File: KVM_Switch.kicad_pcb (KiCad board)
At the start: 4 copper layers, 100 x 70 mm, 118 parts, among them J1 HDMI_A, J2 HDMI_A, J3 HDMI_A, J4 USB_C_Receptacle_USB2.0_16P, J5 USB_C_Receptacle_USB2.0_16P, J6 USB_C_Receptacle_USB2.0_16P, J7 USB_A_Stacked, J8 USB_A_Stacked, SW1 SPST-NO, U1 TPD4E02B04DQA, U10 HD3SS215RTQR, U11 TLV75533PDBV, U12 STM32C031G6Ux, U13 USBLC6-2SC6, U14 TS3USB221AQRSERQ1, U15 USBLC6-2SC6, U16 USB2514B_Bi, U17 USBLC6-2SC6, U18 USBLC6-2SC6, U19 USBLC6-2SC6, U2 TPD4E02B04DQA, U20 USBLC6-2SC6, U3 TPD4E02B04DQA, U4 TPD4E02B04DQA, U5 TPD4E02B04DQA, U6 TPD4E02B04DQA, U7 TPD4E02B04DQA, U8 TPD4E02B04DQA, U9 TPD4E02B04DQA, X1 24MHz

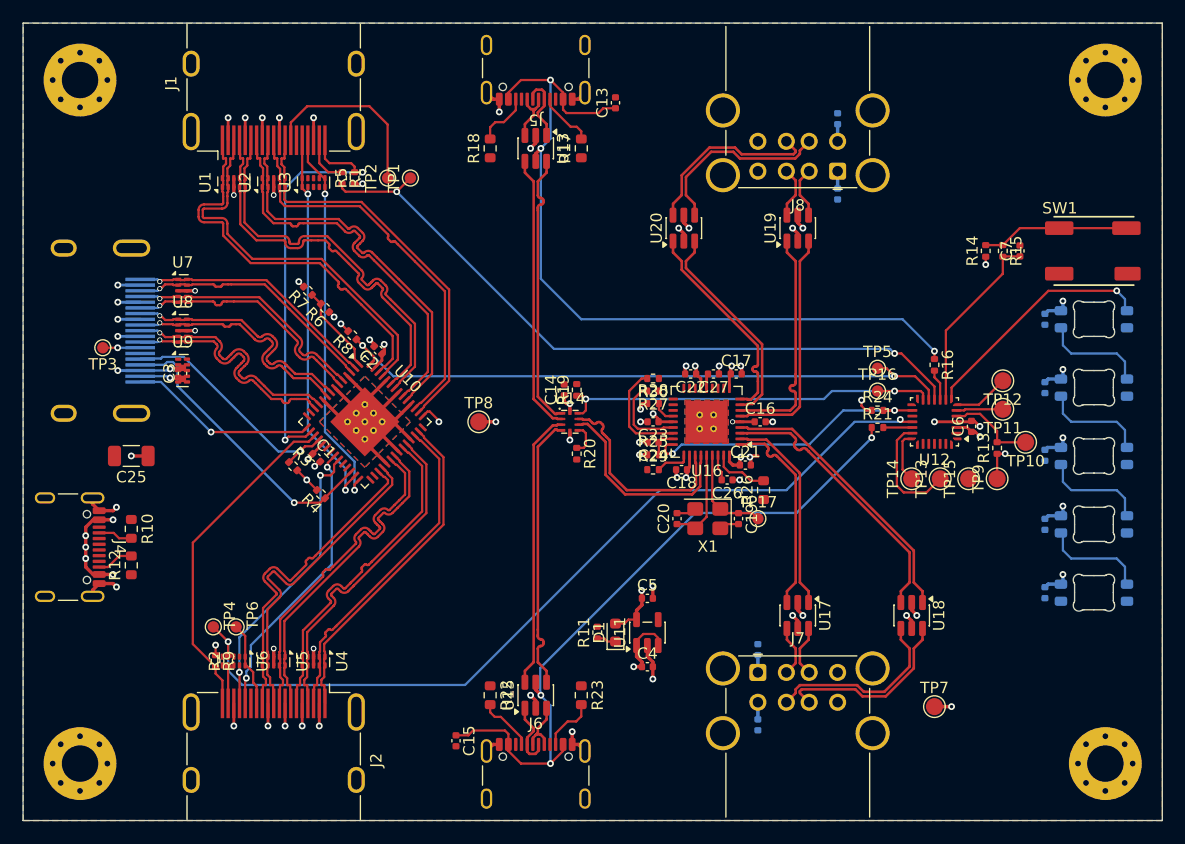
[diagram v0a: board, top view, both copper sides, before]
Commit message: Routed remaining ESD protection
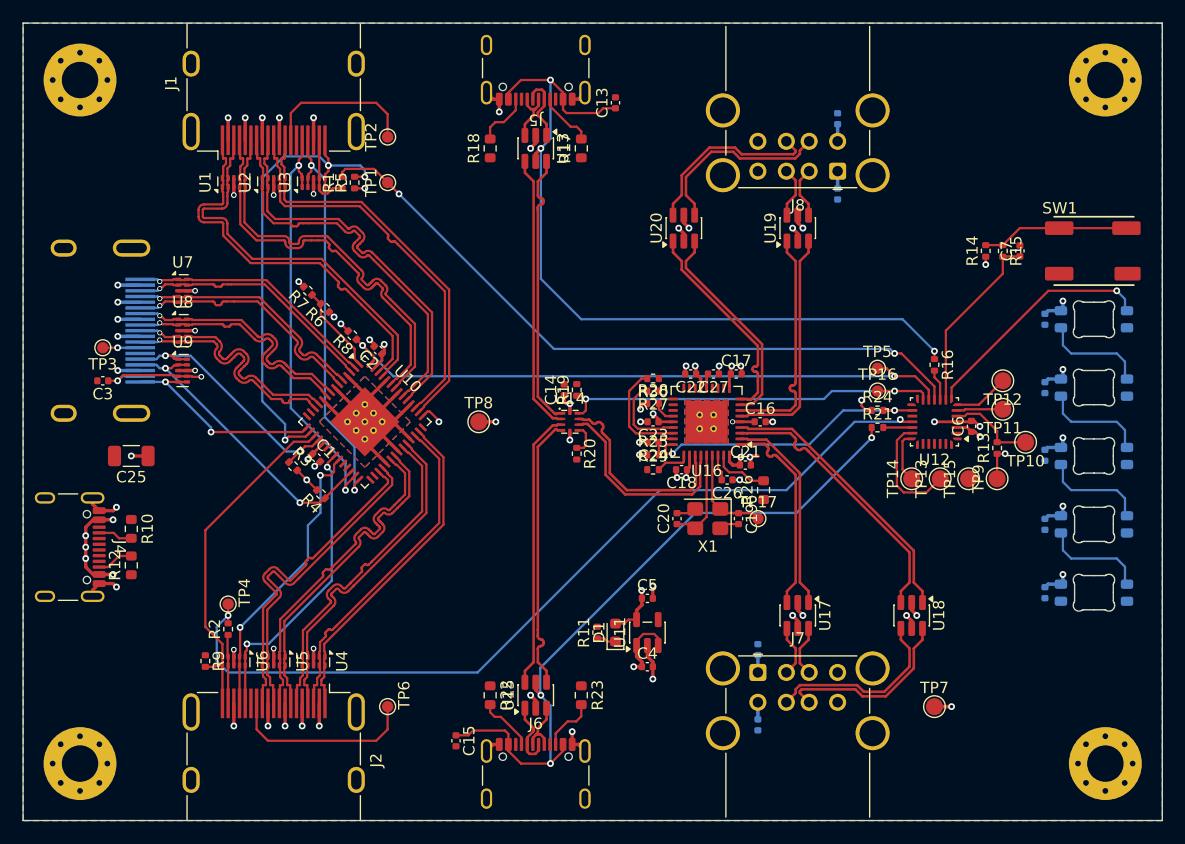
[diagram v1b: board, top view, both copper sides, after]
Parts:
- moved TP6 15.0 mm to (132.0, 125.0)
- moved C3 7.03 mm to (107.0, 96.4), turned to 180 degrees
- moved TP2 3.60 mm to (132.0, 75.0)
- moved R2 2.80 mm to (118.0, 118.2)
- moved TP4 2.39 mm to (118.0, 116.0)
- moved TP1 2.04 mm to (132.0, 79.0)
- moved R9 0.90 mm to (116.0, 121.0)
- moved R1 0.40 mm to (128.0, 79.0), turned to 90 degrees
- moved R5 0.40 mm to (129.1, 79.0)
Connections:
- J1 pad 18: Net-(J1-+5V) -> /HDMI_Switch/HDMI_IN_A/CON_5V
- J2 pad 18: Net-(J2-+5V) -> /HDMI_Switch/HDMI_IN_B/CON_5V
- R1 pad 1: Net-(J1-+5V) -> /HDMI_Switch/HDMI_IN_A/CON_5V
- R2 pad 1: Net-(J2-+5V) -> /HDMI_Switch/HDMI_IN_B/CON_5V
- U3 pad 1: /HDMI_Switch/HDMI_IN_A/CEC -> /HDMI_Switch/HDMI_IN_A/SCL
- U3 pad 10: /HDMI_Switch/HDMI_IN_A/CEC -> /HDMI_Switch/HDMI_IN_A/SCL
- U3 pad 2: /HDMI_Switch/HDMI_IN_A/SCL -> /HDMI_Switch/HDMI_IN_A/SDA
- U3 pad 4: /HDMI_Switch/HDMI_IN_A/SDA -> /HDMI_Switch/HDMI_IN_A/CON_5V
- U3 pad 7: /HDMI_Switch/HDMI_IN_A/SDA -> /HDMI_Switch/HDMI_IN_A/CON_5V
- U3 pad 9: /HDMI_Switch/HDMI_IN_A/SCL -> /HDMI_Switch/HDMI_IN_A/SDA
- U6 pad 1: /HDMI_Switch/HDMI_IN_B/CEC -> /HDMI_Switch/HDMI_IN_B/SCL
- U6 pad 10: /HDMI_Switch/HDMI_IN_B/CEC -> /HDMI_Switch/HDMI_IN_B/SCL
- U6 pad 2: /HDMI_Switch/HDMI_IN_B/SCL -> /HDMI_Switch/HDMI_IN_B/SDA
- U6 pad 4: /HDMI_Switch/HDMI_IN_B/SDA -> /HDMI_Switch/HDMI_IN_B/CON_5V
- U6 pad 7: /HDMI_Switch/HDMI_IN_B/SDA -> /HDMI_Switch/HDMI_IN_B/CON_5V
- U6 pad 9: /HDMI_Switch/HDMI_IN_B/SCL -> /HDMI_Switch/HDMI_IN_B/SDA
- U9 pad 1: /HDMI_Switch/HDMI_OUT/CEC -> /HDMI_Switch/HDMI_OUT/SCL
- U9 pad 10: /HDMI_Switch/HDMI_OUT/CEC -> /HDMI_Switch/HDMI_OUT/SCL
- U9 pad 2: /HDMI_Switch/HDMI_OUT/SCL -> /HDMI_Switch/HDMI_OUT/SDA
- U9 pad 4: /HDMI_Switch/HDMI_OUT/SDA -> VBUS
- U9 pad 7: /HDMI_Switch/HDMI_OUT/SDA -> VBUS
- U9 pad 9: /HDMI_Switch/HDMI_OUT/SCL -> /HDMI_Switch/HDMI_OUT/SDA
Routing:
- net /HDMI_Switch/HDMI_IN_B/CEC: track 7.46 -> 16.6 mm
- net VBUS: track 71.0 -> 77.7 mm, vias 19 -> 20
- net /HDMI_Switch/HDMI_IN_A/CON_5V: track 0.00 -> 6.70 mm
- net /HDMI_Switch/HDMI_IN_B/CON_5V: track 0.00 -> 6.05 mm
- net /HDMI_Switch/HDMI_IN_A/HPD: track 37.8 -> 42.6 mm, vias 2 -> 3
- net Net-(J1-+5V): track 4.34 -> 0.00 mm
- net Net-(J2-+5V): track 3.20 -> 0.00 mm
- net /HDMI_Switch/HDMI_IN_A/SCL: track 33.9 -> 36.8 mm
- net /HDMI_Switch/HDMI_IN_A/CEC: track 16.0 -> 13.7 mm
- net /HDMI_Switch/HDMI_OUT/HPD: track 16.6 -> 18.7 mm, vias 1 -> 2
- net /HDMI_Switch/HDMI_OUT/SCL: track 21.0 -> 23.1 mm, vias 1 -> 2
- net /HDMI_Switch/HDMI_IN_A/SDA: track 33.5 -> 35.5 mm
- net /HDMI_Switch/HDMI_IN_B/SCL: track 25.4 -> 26.5 mm
- net /HDMI_Switch/DET_B: track 75.9 -> 76.9 mm
- net /HDMI_Switch/DET_A: track 62.5 -> 61.6 mm
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
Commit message: Rerouted HDMI TMDS
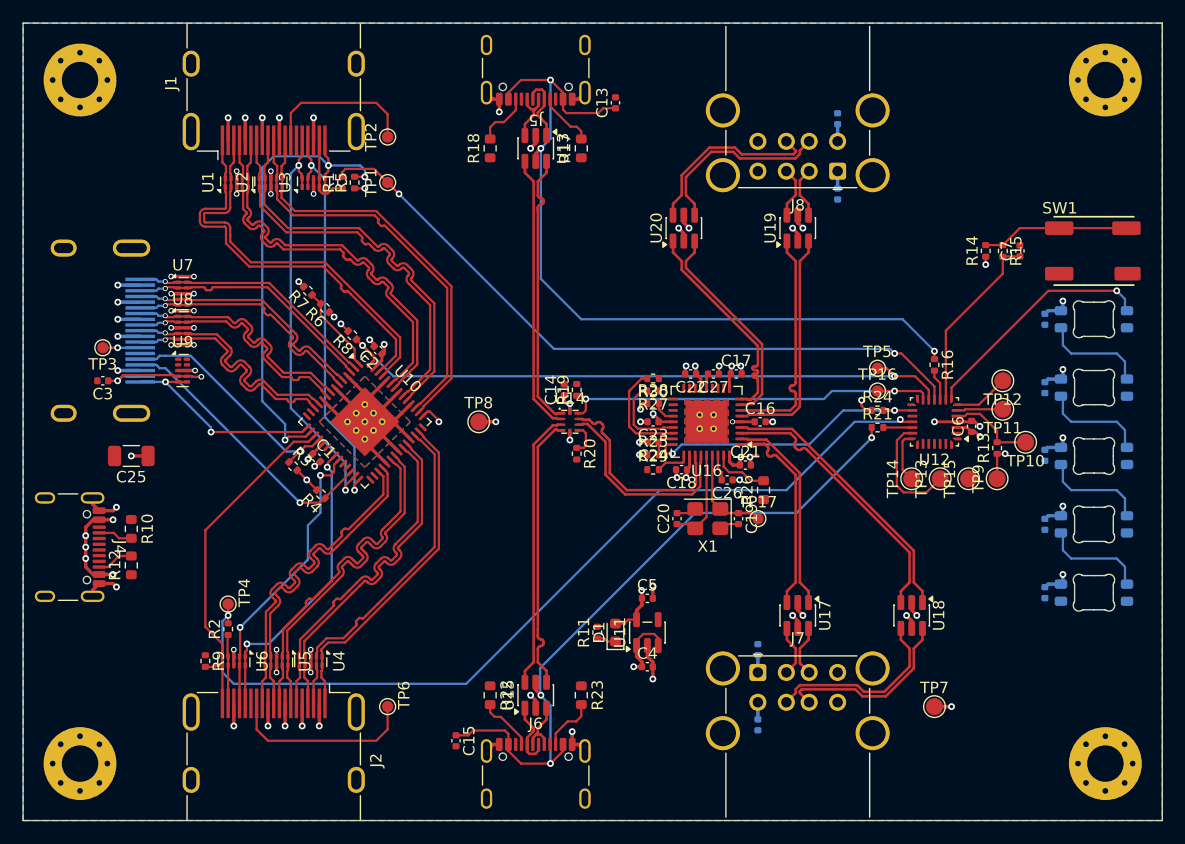
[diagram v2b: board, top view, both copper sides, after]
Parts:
- moved U1 0.25 mm to (118.8, 79.0)
- moved U2 0.25 mm to (121.8, 79.0)
- moved U4 0.25 mm to (125.2, 121.0)
- moved U5 0.25 mm to (122.2, 121.0)
- moved U7 0.25 mm to (114.0, 88.8)
- moved U8 0.25 mm to (114.0, 91.8)
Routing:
- net GND: track 115.3 -> 124.4 mm, vias 54 -> 66
- net /HDMI_Switch/HDMI_OUT/SDA: track 26.7 -> 24.7 mm, vias 2 -> 1
- net /HDMI_Switch/HDMI_OUT/SCL: track 23.1 -> 21.1 mm, vias 2 -> 1
- net /USB_Hub/USB_DOWN_2/USB2_DP: track 18.8 -> 19.6 mm
- net /HDMI_Switch/DET_B: track 76.9 -> 77.6 mm
- net /HDMI_Switch/HDMI_IN_A/HPD: track 42.6 -> 43.1 mm

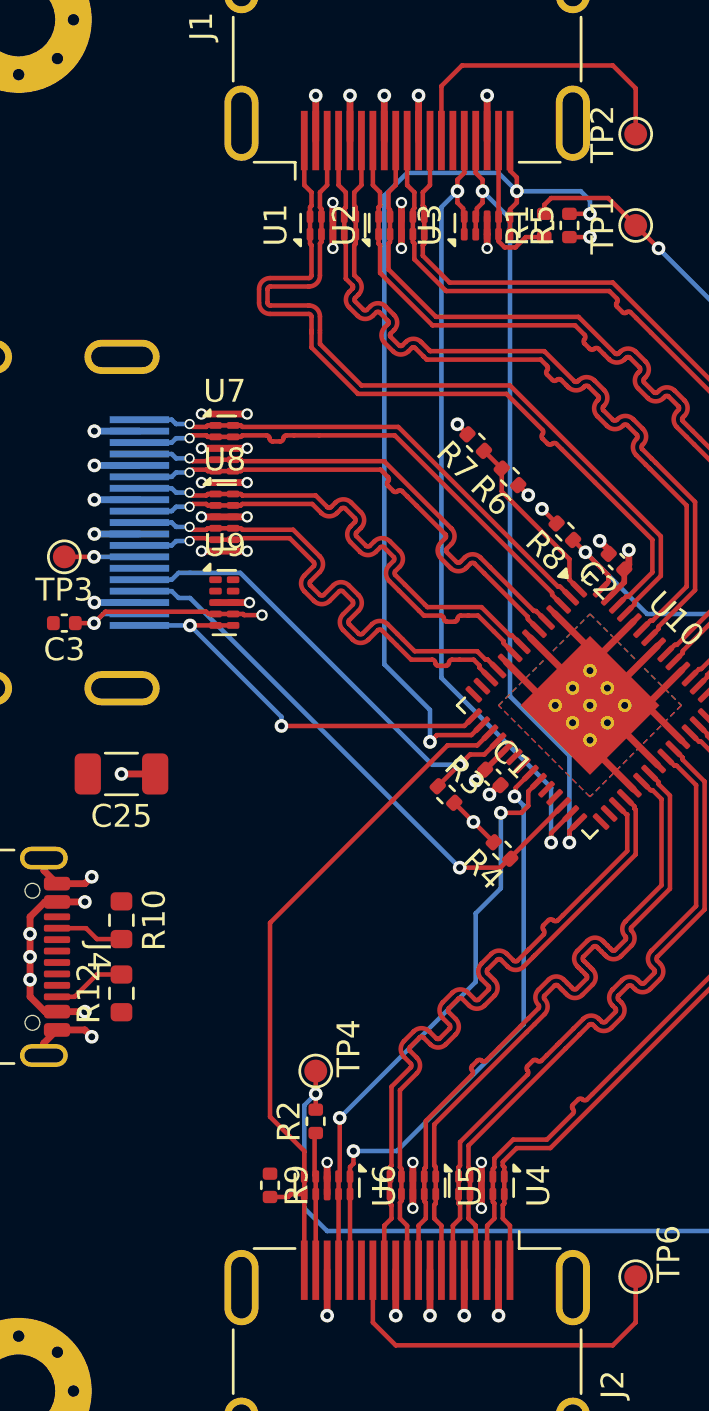
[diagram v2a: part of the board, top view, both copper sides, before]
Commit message: i2c rerouted
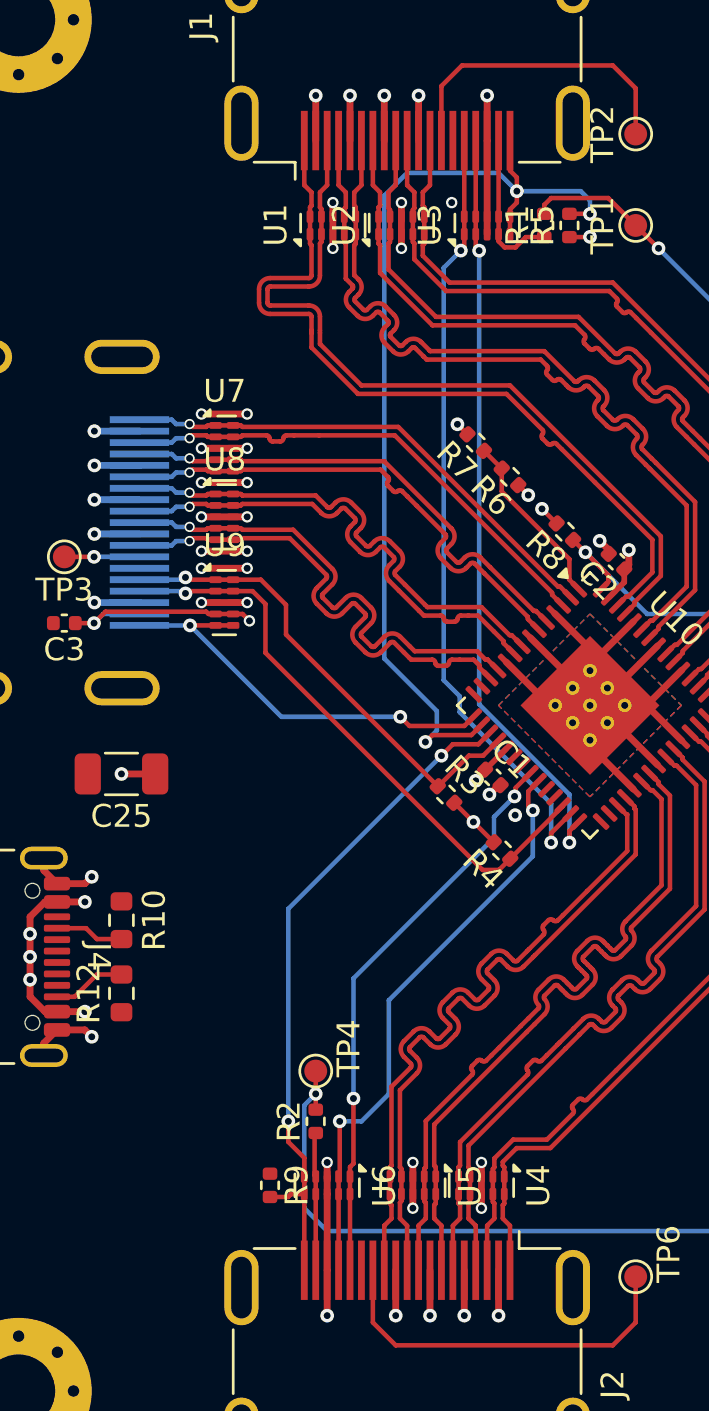
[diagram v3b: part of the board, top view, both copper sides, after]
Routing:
- net GND: track 124.4 -> 133.0 mm, vias 66 -> 70
- net /HDMI_Switch/HDMI_IN_A/SCL: track 36.8 -> 34.7 mm
- net /HDMI_Switch/HDMI_IN_A/SDA: track 35.5 -> 33.5 mm
- net /HDMI_Switch/HDMI_IN_B/SCL: track 26.5 -> 25.0 mm
- net /HDMI_Switch/HDMI_OUT/SDA: track 24.7 -> 26.1 mm
- net /HDMI_Switch/HDMI_IN_B/HPD: track 30.4 -> 29.7 mm, vias 0 -> 2
- net /HDMI_Switch/HDMI_IN_A/HPD: track 43.1 -> 43.6 mm

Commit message: Fix naming typo: KVM_Swtich -> KVM_Switch
Renamed the footprint library folder library/KVM_Swtich.pretty to
library/KVM_Switch.pretty and the 3D model swtich_smd_6x6mm.step to
switch_smd_6x6mm.step, and updated every reference across
fp-lib-table, sym-lib-table, the schematics, symbols.kicad_sym, and
the PCB. Also fixed a stray "Swtich A to C" text label.
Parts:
- D2, D3, D4, D5, D6: footprint KVM_Swtich:LED_SK6812MINI-E_3.2x2.8mm_P1.5mm_ReverseMount -> KVM_Switch:LED_SK6812MINI-E_3.2x2.8mm_P1.5mm_ReverseMount
- J7, J8: footprint KVM_Swtich:USB_A_Wuerth_61400826021_Horizontal_Stacked -> KVM_Switch:USB_A_Wuerth_61400826021_Horizontal_Stacked
- SW1: footprint KVM_Swtich:EVQ-Q2K03W -> KVM_Switch:EVQ-Q2K03W
- U14: footprint KVM_Swtich:TS3USB221AQRSERQ1 -> KVM_Switch:TS3USB221AQRSERQ1
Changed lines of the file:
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@@
 		)
 	)
-	(footprint "KVM_Swtich:EVQ-Q2K03W"
+	(footprint "KVM_Switch:EVQ-Q2K03W"
 		(locked yes)
 		(layer "F.Cu")
@@
 		)
 		(embedded_fonts no)
-		(model "${KIPRJMOD}/library/3d_models/swtich_smd_6x6mm.step"
+		(model "${KIPRJMOD}/library/3d_models/switch_smd_6x6mm.step"
 			(offset
 				(xyz 0 0 0)
@@
 		)
 	)
-	(footprint "KVM_Swtich:TS3USB221AQRSERQ1"
+	(footprint "KVM_Switch:TS3USB221AQRSERQ1"
 		(locked yes)
 		(layer "F.Cu")
@@
 		)
 	)
-	(footprint "KVM_Swtich:USB_A_Wuerth_61400826021_Horizontal_Stacked"
+	(footprint "KVM_Switch:USB_A_Wuerth_61400826021_Horizontal_Stacked"
 		(locked yes)
 		(layer "F.Cu")
@@
 		)
 	)
-	(footprint "KVM_Swtich:USB_A_Wuerth_61400826021_Horizontal_Stacked"
+	(footprint "KVM_Switch:USB_A_Wuerth_61400826021_Horizontal_Stacked"
 		(locked yes)
 		(layer "F.Cu")
@@
 		)
 	)
-	(footprint "KVM_Swtich:LED_SK6812MINI-E_3.2x2.8mm_P1.5mm_ReverseMount"
+	(footprint "KVM_Switch:LED_SK6812MINI-E_3.2x2.8mm_P1.5mm_ReverseMount"
 		(layer "B.Cu")
 		(at 194 103 180)
@@
 		)
 	)
-	(footprint "KVM_Swtich:LED_SK6812MINI-E_3.2x2.8mm_P1.5mm_ReverseMount"
+	(footprint "KVM_Switch:LED_SK6812MINI-E_3.2x2.8mm_P1.5mm_ReverseMount"
 		(layer "B.Cu")
 		(at 194 109 180)
@@
 		)
 	)
-	(footprint "KVM_Swtich:LED_SK6812MINI-E_3.2x2.8mm_P1.5mm_ReverseMount"
+	(footprint "KVM_Switch:LED_SK6812MINI-E_3.2x2.8mm_P1.5mm_ReverseMount"
 		(layer "B.Cu")
 		(at 194 91 180)
@@
 		)
 	)
-	(footprint "KVM_Swtich:LED_SK6812MINI-E_3.2x2.8mm_P1.5mm_ReverseMount"
+	(footprint "KVM_Switch:LED_SK6812MINI-E_3.2x2.8mm_P1.5mm_ReverseMount"
 		(layer "B.Cu")
 		(at 194 115 180)
@@
 		)
 	)
-	(footprint "KVM_Swtich:LED_SK6812MINI-E_3.2x2.8mm_P1.5mm_ReverseMount"
+	(footprint "KVM_Switch:LED_SK6812MINI-E_3.2x2.8mm_P1.5mm_ReverseMount"
 		(layer "B.Cu")
 		(at 194 97 180)

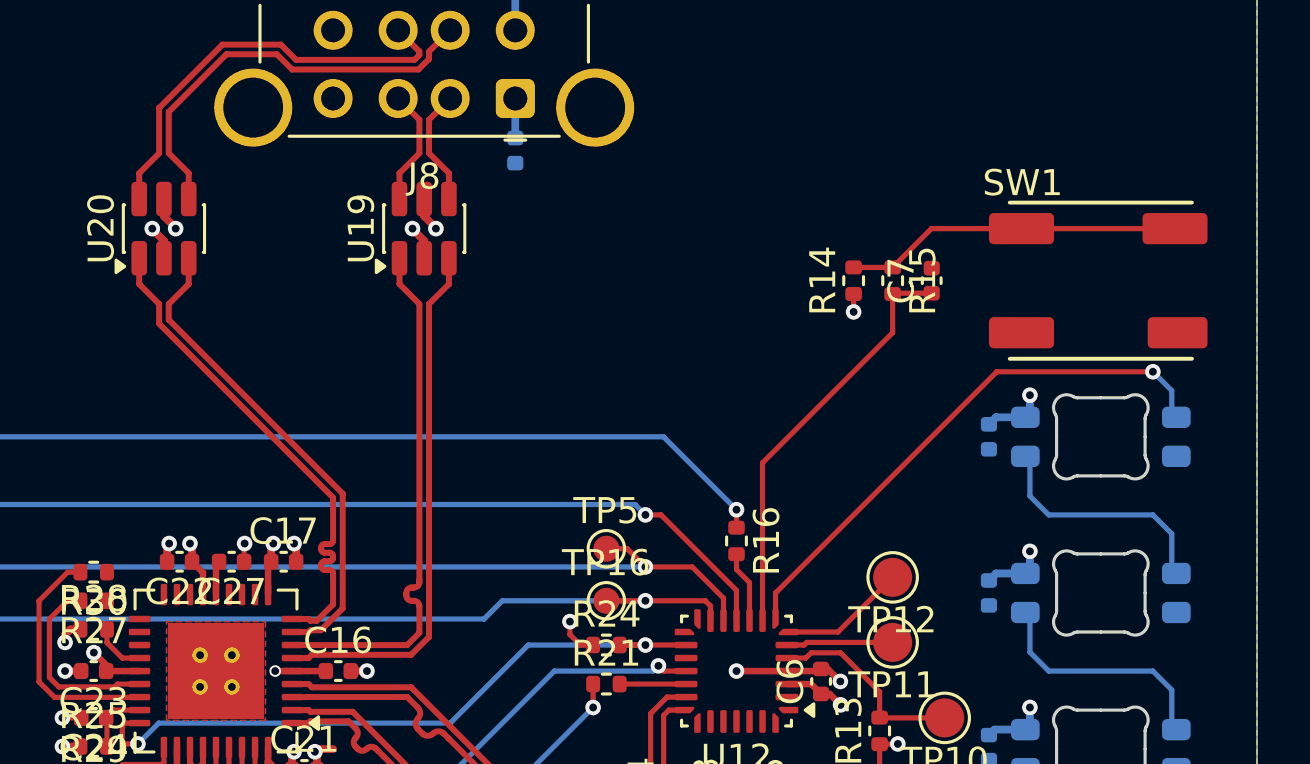
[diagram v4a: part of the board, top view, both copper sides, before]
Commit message: Updated custom rules & Changed switch
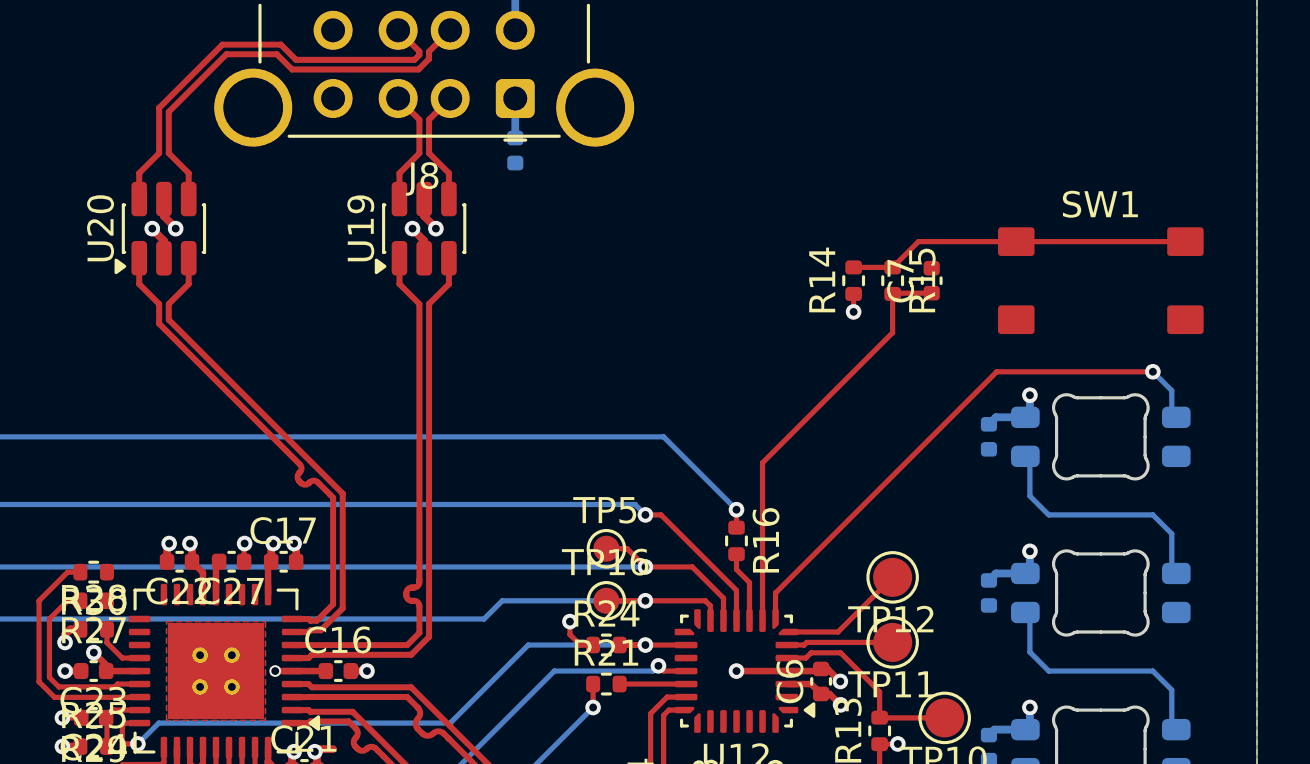
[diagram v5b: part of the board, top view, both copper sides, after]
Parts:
- SW1: footprint KVM_Switch:EVQ-Q2K03W -> KVM_Switch:UK-B0206-G5-250-JZ
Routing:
- net /USB_Hub/USB_DOWN_2/USB2_DP: track 19.6 -> 18.8 mm
